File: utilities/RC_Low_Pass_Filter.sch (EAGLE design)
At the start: 2 parts

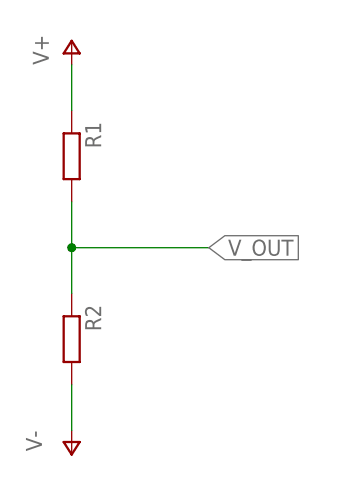
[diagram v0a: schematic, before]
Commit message: added RC low pass filter, and updated paypal button???
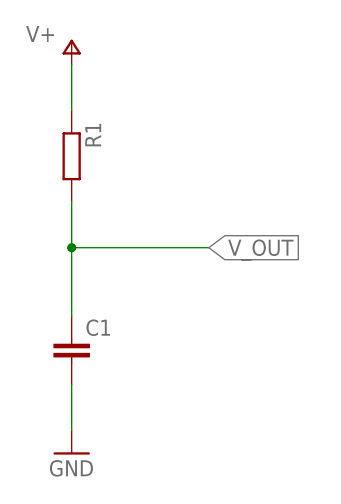
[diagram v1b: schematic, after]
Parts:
- removed R2: (no value), rcl:R-EU_R0805
- added C1: (no value), rcl:C-EU025-024X044
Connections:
- removed net V-: R2.2
- new net GND: C1.2
- net V_OUT: now also C1.1; no longer R2.1
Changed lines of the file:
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@@
 <parts>
 <part name="R1" library="rcl" deviceset="R-EU_" device="R0805"/>
-<part name="R2" library="rcl" deviceset="R-EU_" device="R0805"/>
+<part name="C1" library="rcl" deviceset="C-EU" device="025-024X044"/>
 <part name="P+1" library="supply1" deviceset="V+" device=""/>
-<part name="P-1" library="supply1" deviceset="V-" device=""/>
+<part name="GND1" library="supply1" deviceset="GND" device=""/>
 </parts>
 <sheets>
@@
 <instances>
 <instance part="R1" gate="G$1" x="7.62" y="60.96" rot="R270"/>
-<instance part="R2" gate="G$1" x="7.62" y="40.64" rot="R270"/>
-<instance part="P+1" gate="1" x="7.62" y="73.66"/>
-<instance part="P-1" gate="1" x="7.62" y="27.94"/>
+<instance part="C1" gate="G$1" x="7.62" y="40.64"/>
+<instance part="P+1" gate="1" x="7.62" y="73.66" smashed="yes">
+<attribute name="VALUE" x="2.54" y="73.66" size="1.778" layer="96"/>
+</instance>
+<instance part="GND1" gate="1" x="7.62" y="27.94"/>
 </instances>
 <busses>
 </busses>
 <nets>
-<net name="V-" class="0">
-<segment>
-<pinref part="R2" gate="G$1" pin="2"/>
-<pinref part="P-1" gate="1" pin="V-"/>
-<wire x1="7.62" y1="30.48" x2="7.62" y2="35.56" width="0.1524" layer="91"/>
-</segment>
-</net>
 <net name="V+" class="0">
 <segment>
@@
 <segment>
 <pinref part="R1" gate="G$1" pin="2"/>
-<pinref part="R2" gate="G$1" pin="1"/>
+<pinref part="C1" gate="G$1" pin="1"/>
 <wire x1="7.62" y1="55.88" x2="7.62" y2="50.8" width="0.1524" layer="91"/>
-<wire x1="7.62" y1="50.8" x2="7.62" y2="45.72" width="0.1524" layer="91"/>
+<wire x1="7.62" y1="50.8" x2="7.62" y2="43.18" width="0.1524" layer="91"/>
 <wire x1="7.62" y1="50.8" x2="22.86" y2="50.8" width="0.1524" layer="91"/>
 <junction x="7.62" y="50.8"/>
@@
 </segment>
 </net>
+<net name="GND" class="0">
+<segment>
+<pinref part="C1" gate="G$1" pin="2"/>
+<wire x1="7.62" y1="30.48" x2="7.62" y2="35.56" width="0.1524" layer="91"/>
+<pinref part="GND1" gate="1" pin="GND"/>
+</segment>
+</net>
